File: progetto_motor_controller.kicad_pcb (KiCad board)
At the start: 4 copper layers, 66 x 75 mm, 114 parts, among them J1 USB_B_Micro, J2 Conn_01x06, J3 Conn_01x04, J4 Screw_Terminal_01x03, J5 Conn_01x05, J6 Conn_02x10_Odd_Even, J7 Conn_01x02, J8 Screw_Terminal_01x02, J9 Conn_01x03, Q1 BSC022N04LSATMA1, Q2 BSC022N04LSATMA1, Q3 BSC022N04LSATMA1, Q4 BSC022N04LSATMA1, Q5 BSC022N04LSATMA1, Q6 BSC022N04LSATMA1, Q7 BSC022N04LSATMA1, Q8 BSC022N04LSATMA1, U1 STM32F303RETx, U2 SN65HVD253D, U3 USBLC6-2P6, U4 TMC6140, U5 TSC2011, U6 TSC2011, U7 MYRGC07506_1, U8 TLV707, U9 TLV707, Y1 16MHz

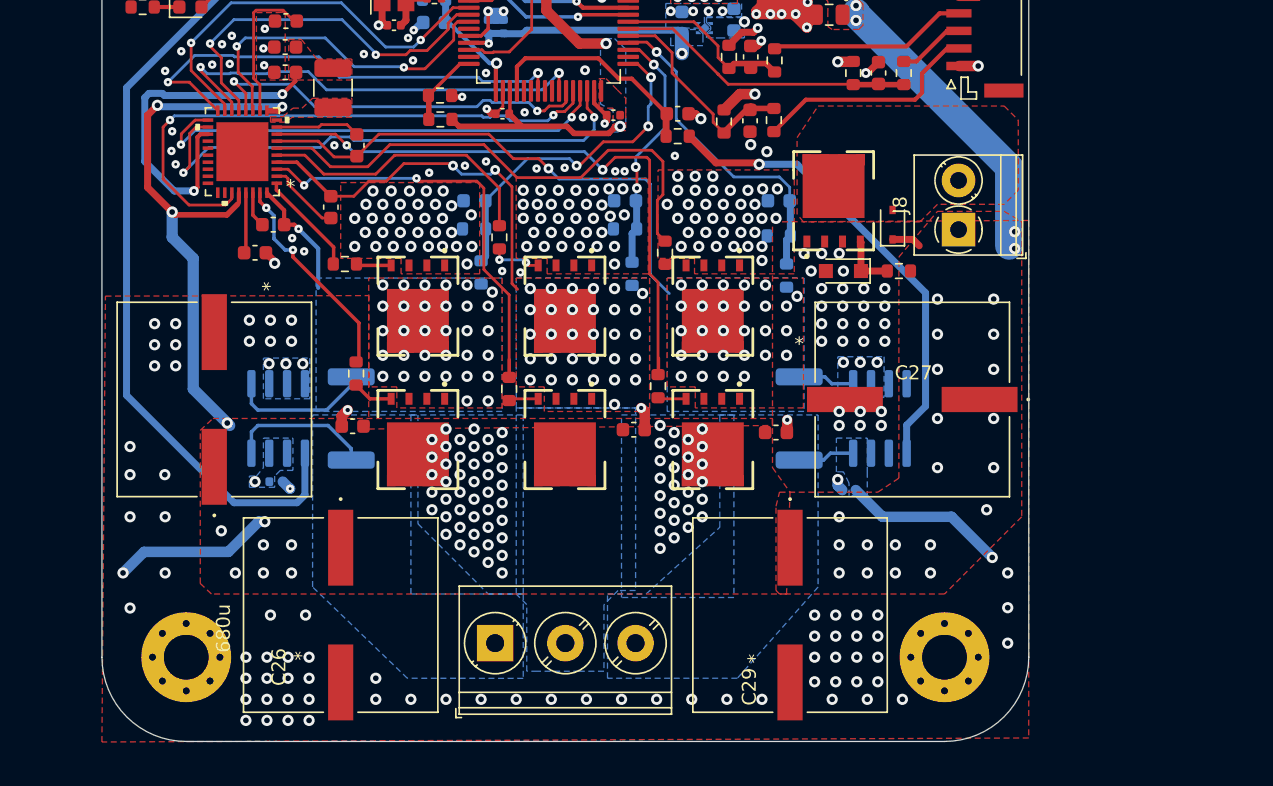
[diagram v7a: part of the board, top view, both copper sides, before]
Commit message: changed mosfet spacing
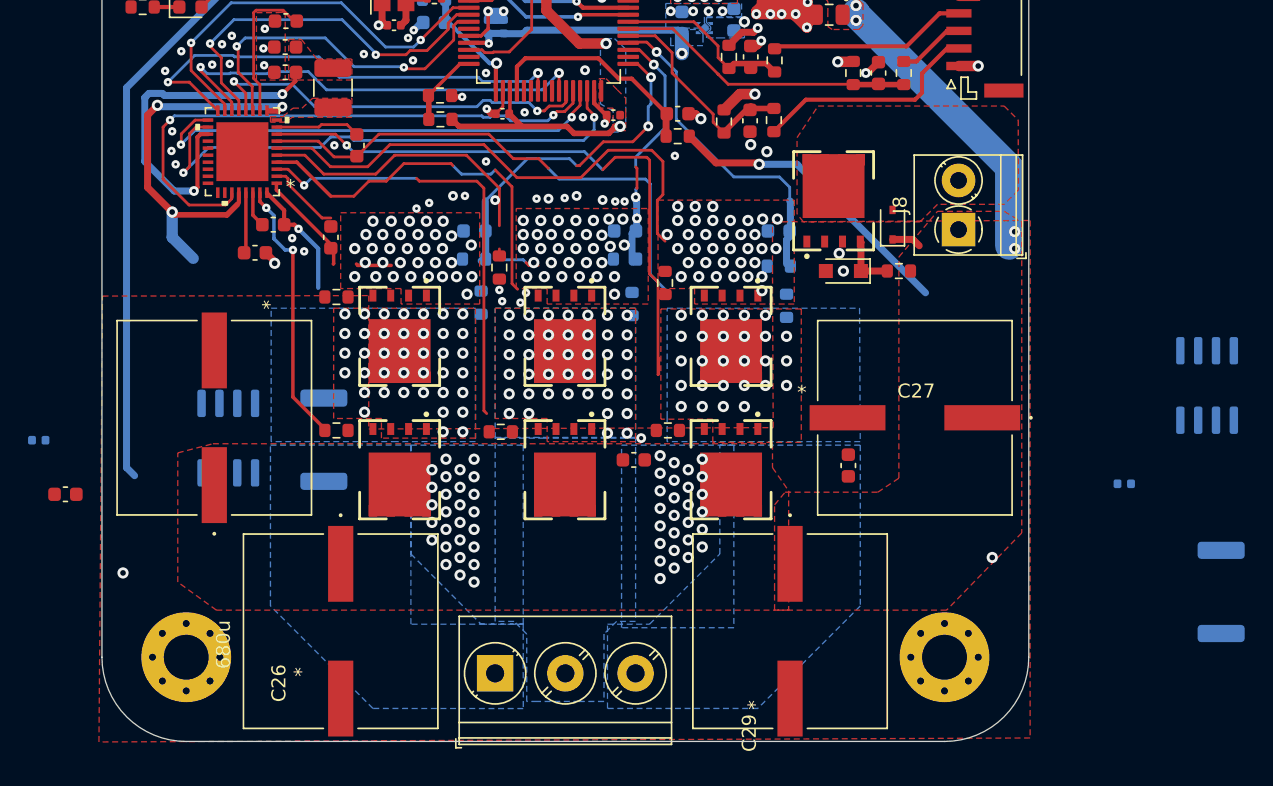
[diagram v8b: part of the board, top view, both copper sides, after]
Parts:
- moved R11 32.5 mm to (162.7, 141.3)
- moved U6 23.4 mm to (161.7, 126.7)
- moved C20 21.0 mm to (80.4, 134.4)
- moved C16 19.6 mm to (155.8, 133.7)
- moved C17 17.2 mm to (78.5, 130.6)
- moved C23 5.66 mm to (136.2, 132.3), turned to 90 degrees
- moved R14 4.29 mm to (99.7, 129.8), turned to 180 degrees
- moved U5 3.82 mm to (92.0, 130.4)
- moved R16 3.23 mm to (123.3, 129.8), turned to 180 degrees
- moved R24 3.11 mm to (111.4, 129.9), turned to 180 degrees
- moved Q2 2.51 mm to (104.2, 132.7)
- moved Q3 2.51 mm to (104.2, 123.2)
- moved Q4 2.51 mm to (127.8, 132.7)
- moved Q5 2.51 mm to (127.8, 123.2)
- moved R10 2.47 mm to (98.8, 130.5)
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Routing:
- net 3V3_VDAA: track 75.8 -> 53.2 mm, vias 6 -> 4
- net HB: track 31.2 -> 10.7 mm
- net /Inverter/LA_G: track 0.00 -> 20.5 mm
- net HA: track 44.8 -> 24.3 mm
- net /Inverter/LB_G: track 3.71 -> 24.2 mm
- net /Inverter/C1_OUT: track 65.2 -> 52.1 mm
- net VDD: track 64.5 -> 51.5 mm, vias 105 -> 61
- net /Inverter/C2_OUT: track 33.4 -> 21.4 mm
- net PH_C: track 10.3 -> 0.00 mm
- net PH_C_CS: track 18.8 -> 8.72 mm, vias 33 -> 40
- net PH_A_CS: track 41.6 -> 37.6 mm, vias 29 -> 28
- net PH_A: track 4.05 -> 0.00 mm
- net HC: track 15.4 -> 19.2 mm
- net GND: track 84.5 -> 81.5 mm, vias 318 -> 211
- net /Inverter/HC_G: track 2.90 -> 0.00 mm
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- removed copper zone on In1.Cu, net VDD
